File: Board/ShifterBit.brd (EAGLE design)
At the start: 27.2 x 61 mm, 13 parts

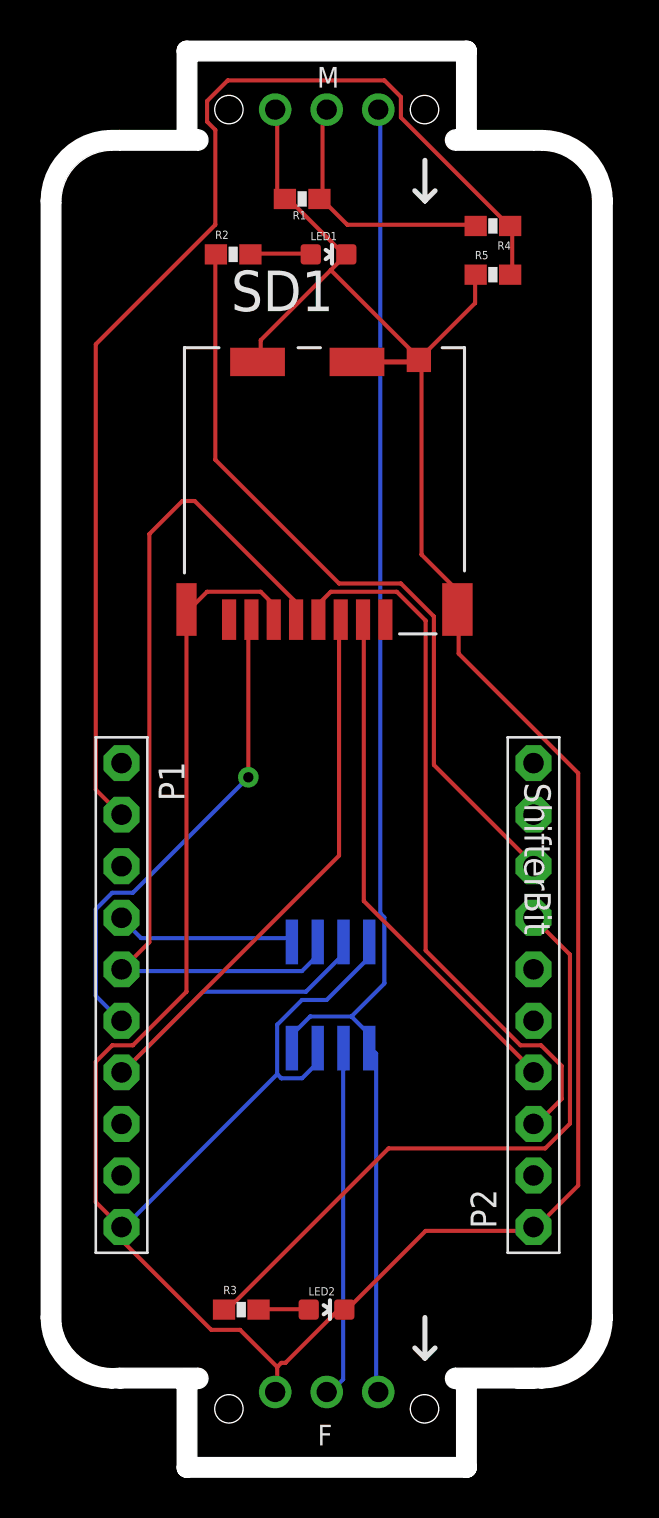
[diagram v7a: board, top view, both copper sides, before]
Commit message: use 1206 packages
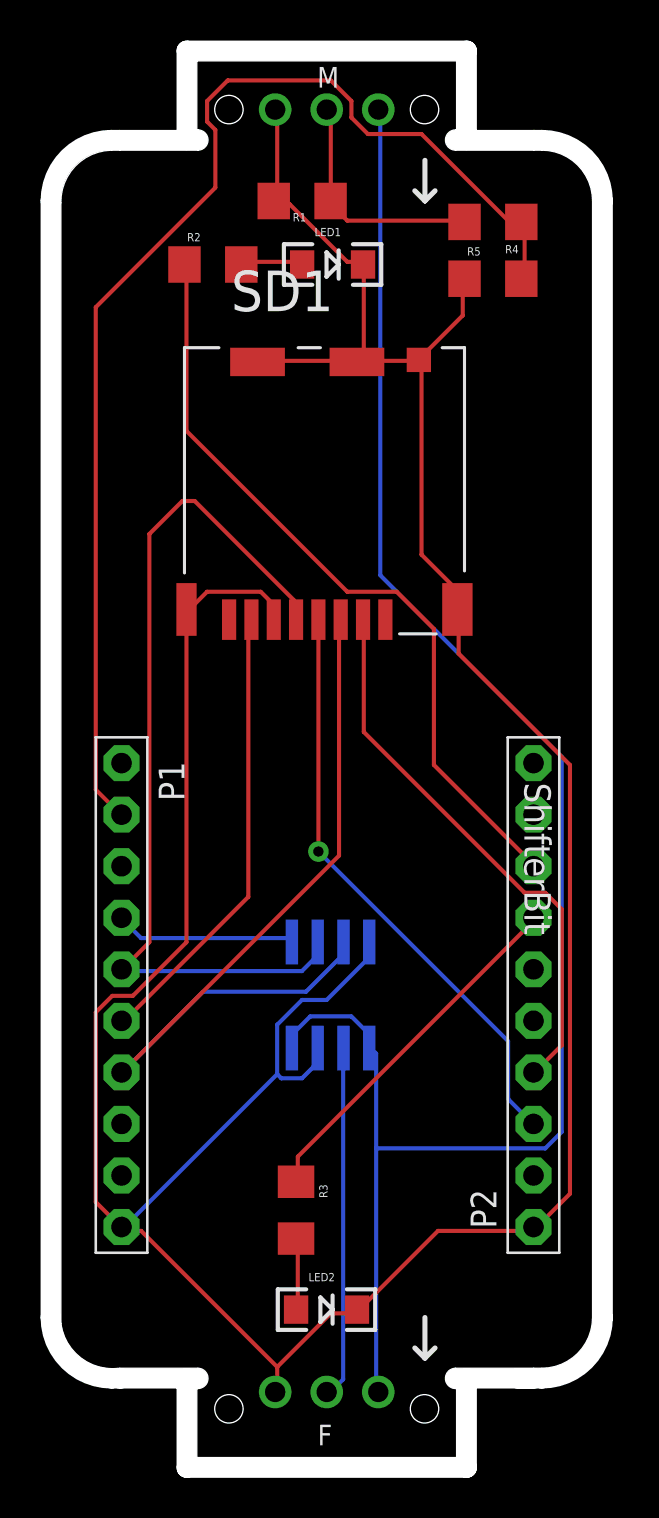
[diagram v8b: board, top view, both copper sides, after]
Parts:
- LED1, LED2: value (none) -> GREEN; device SparkFun-LED:LED-0603 -> SparkFun-LED:LED-1206
- R1: device LITTLEBITS:RES-0603 -> LITTLEBITS:RES-1206
- R2, R3, R4, R5: device SparkFun-Passives:0603-RES -> SparkFun-Passives:1206
- moved R3 5.59 mm to (11.7, 12.4), turned to 270 degrees
- moved R2 1.12 mm to (7.60, 59.0)
- moved LED1 0.54 mm to (13.5, 59.0), turned to 0 degrees
- moved R4 0.20 mm to (21.4, 61.1)
- moved R5 0.20 mm to (21.4, 58.3)
- moved R1 0.10 mm to (12.0, 62.1)
- turned LED2 to 0 degrees
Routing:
- net VCC: track 68.5 -> 86.7 mm
- net D4: track 31.7 -> 17.9 mm
- net 3V: track 35.7 -> 29.2 mm, vias 0 -> 1
- net GND: track 167.8 -> 164.7 mm
- net D15: track 25.8 -> 27.6 mm
- net D12: track 24.1 -> 22.5 mm, vias 1 -> 0
- net N$9: track 2.48 -> 3.63 mm
- net SIG_IN: track 12.8 -> 11.7 mm
- net A1: track 59.7 -> 60.6 mm
